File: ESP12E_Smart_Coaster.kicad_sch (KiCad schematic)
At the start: 33 parts, among them J1 SPI_Header, J2 MLX90614 Temp Sensor, J3 GPIO_Header, Q1 SI2302, SW1 SW_SPDT, SW2 SW_Push, U1 T6845C_Module, U2 ESP-12E, U3 AMS1117-3.3

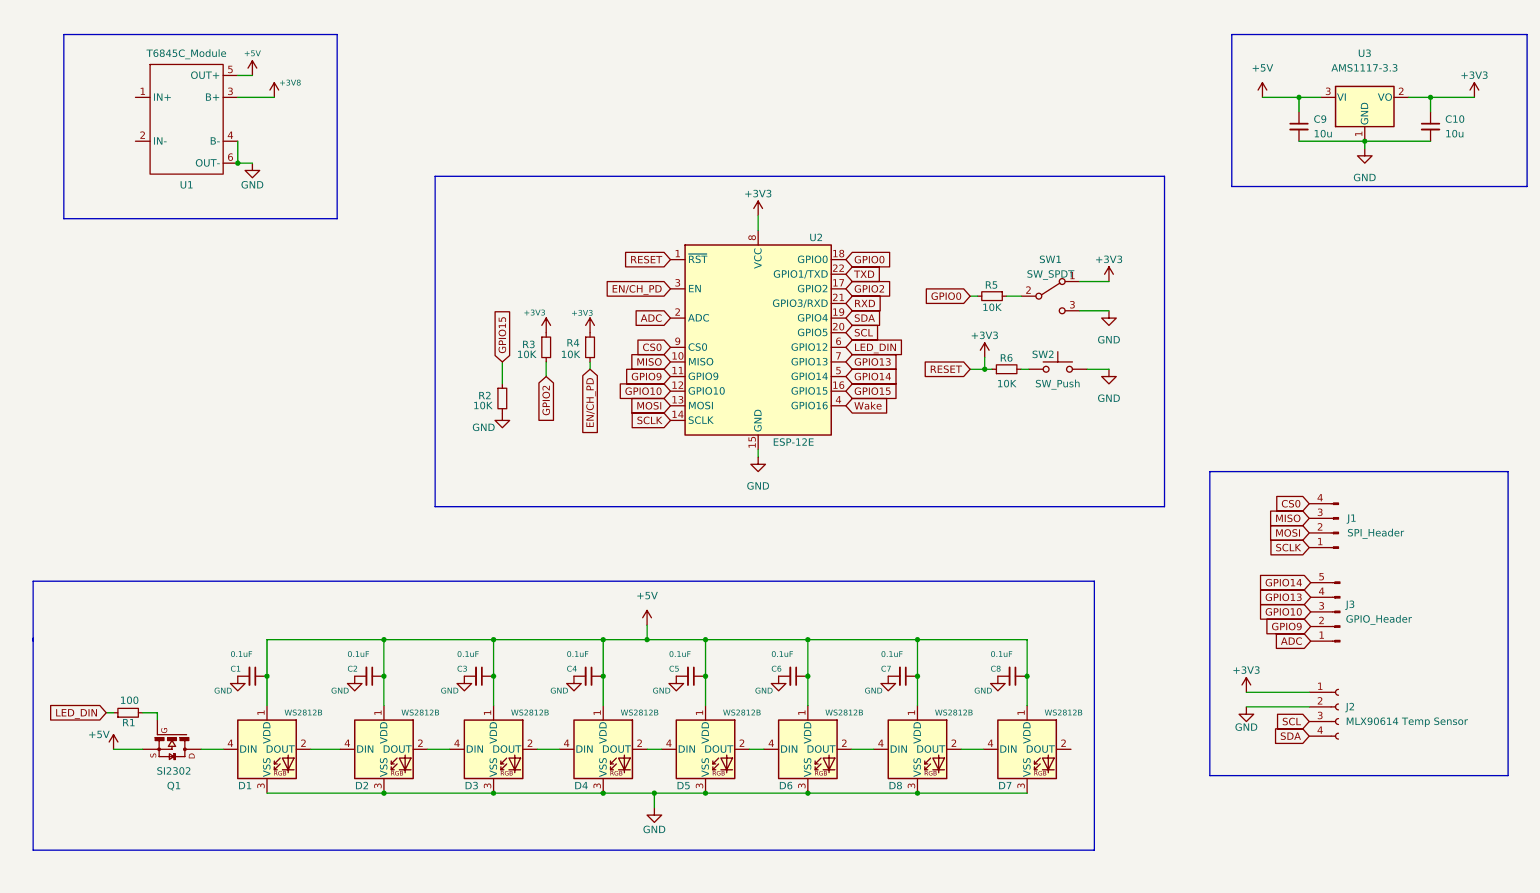
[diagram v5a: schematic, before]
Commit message: Started component placement
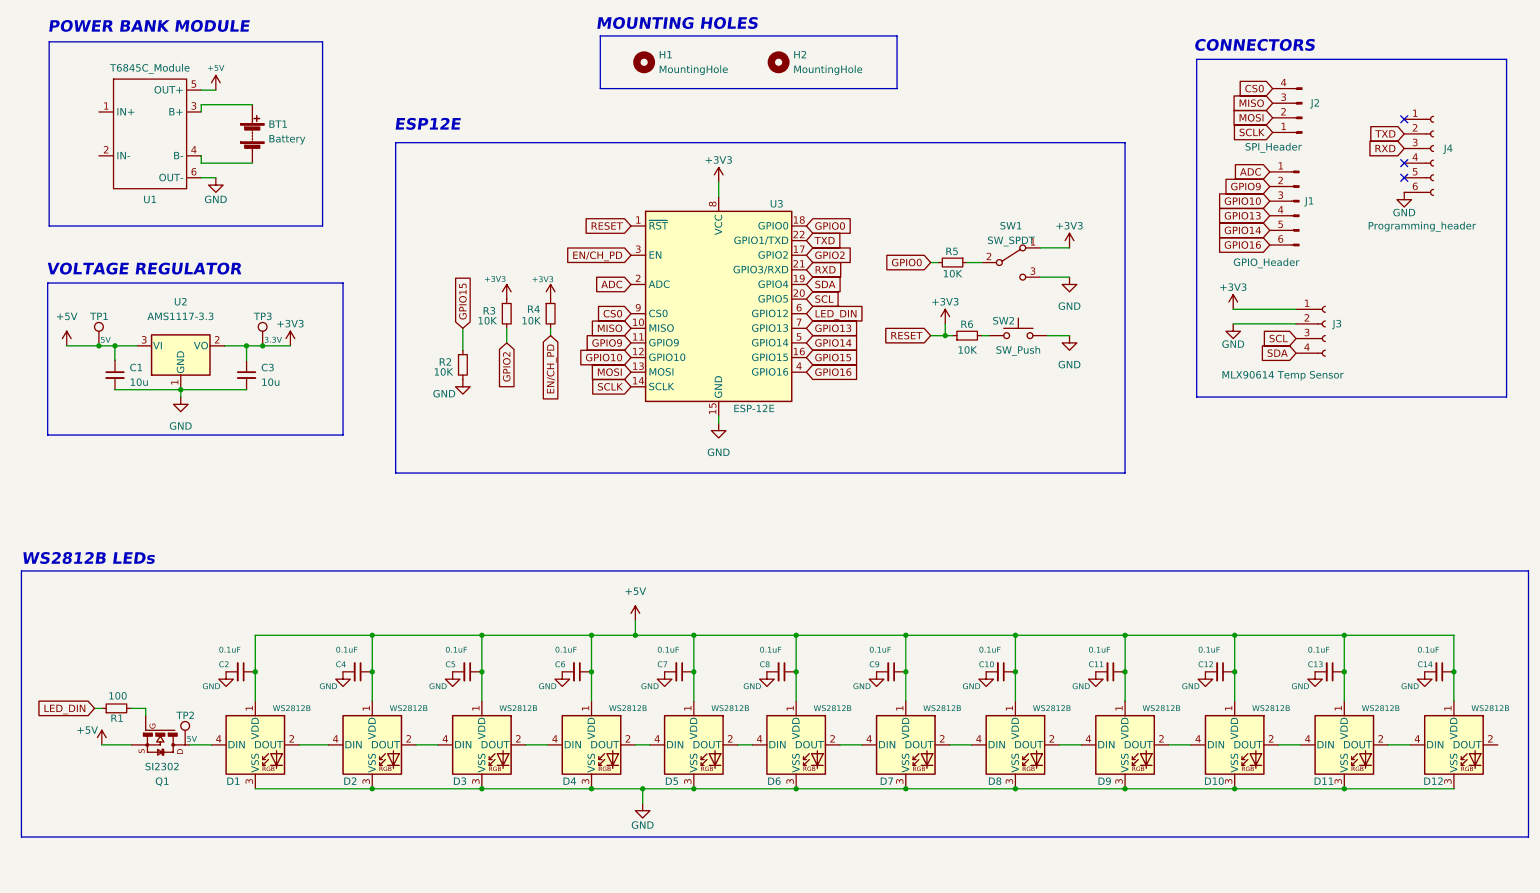
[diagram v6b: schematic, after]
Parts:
- removed J3: GPIO_Header, Connector_PinHeader_2.54mm:PinHeader_1x05_P2.54mm_Vertical, symbol Connector:Conn_01x05_Male
- added BT1: Battery, Battery:BatteryHolder_Keystone_1042_1x18650, symbol Device:Battery
- added C11, C12, C13, C14: 0.1uF, Capacitor_SMD:C_1206_3216Metric_Pad1.33x1.80mm_HandSolder, symbol Device:C_Small
- added D10, D11, D12, D9: WS2812B, LED_SMD:LED_WS2812B_PLCC4_5.0x5.0mm_P3.2mm, symbol LED:WS2812B
- added H1, H2: MountingHole, MountingHole:MountingHole_3.2mm_M3, symbol Mechanical:MountingHole
- added J1: GPIO_Header, Connector_PinHeader_2.54mm:PinHeader_1x06_P2.54mm_Vertical, symbol Connector:Conn_01x06_Male
- added J4: Programming_header, Connector_PinSocket_2.54mm:PinSocket_1x06_P2.54mm_Vertical, symbol Connector:Conn_01x06_Female
- added TP1, TP2: 5V, TestPoint:TestPoint_Loop_D2.54mm_Drill1.5mm_Beaded, symbol Connector:TestPoint
- added TP3: 3.3V, TestPoint:TestPoint_Loop_D2.54mm_Drill1.5mm_Beaded, symbol Connector:TestPoint
- J3: renamed from J2; footprint Connector_PinHeader_2.54mm:PinHeader_1x04_P2.54mm_Vertical -> Connector_JST:JST_XH_B4B-XH-A_1x04_P2.50mm_Vertical
- U1: footprint Button_Switch_SMD:SW_Push_SPST_NO_Alps_SKRK -> Power_Bank_Module:T6845C_Module
- renumbered C9 to C1, C8 to C10, C1 to C2, C10 to C3, C2 to C4, C3 to C5, C4 to C6, C5 to C7, C6 to C8, C7 to C9, J1 to J2, U3 to U2, U2 to U3
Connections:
- net +3V3: now also TP3.1
- net +5V: now also C11.1, C12.1, C13.1, C14.1, D10.1 (VDD), D11.1 (VDD), D12.1 (VDD), D9.1 (VDD), TP1.1
- net ADC: now also J1.1 (Pin_1)
- net GND: now also C11.2, C12.2, C13.2, C14.2, D10.3 (VSS), D11.3 (VSS), D12.3 (VSS), D9.3 (VSS), J4.6 (Pin_6); no longer U1.4 (B-)
- net GPIO10: now also J1.3 (Pin_3)
- net GPIO13: now also J1.4 (Pin_4)
- net GPIO14: now also J1.5 (Pin_5)
- net GPIO9: now also J1.2 (Pin_2)
- net RXD: now also J4.3 (Pin_3)
- net TXD: now also J4.2 (Pin_2)
- net at D8.2 (DOUT): now also D9.4 (DIN)
- net +3V8: no longer names the net of U1.3 (B+)
- net +3V8: now also BT1.1 (+)
- net Wake renamed GPIO16
- net GPIO16: now also J1.6 (Pin_6)
- new net: D11.2 (DOUT), D12.4 (DIN)
- new net: D10.2 (DOUT), D11.4 (DIN)
- new net: D10.4 (DIN), D9.2 (DOUT)
- new net: BT1.2 (-), U1.4 (B-)
- no-connect marks 0 -> 3
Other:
- note added: "CONNECTORS"
- note added: "ESP12E"
- note added: "MOUNTING HOLES"
- note added: "POWER BANK MODULE"
- note added: "VOLTAGE REGULATOR"
- note added: "WS2812B LEDs"
- moved on the sheet: C1, C10, C2, C3, C4, C5, C6, C7, C8, C9, D1, D2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

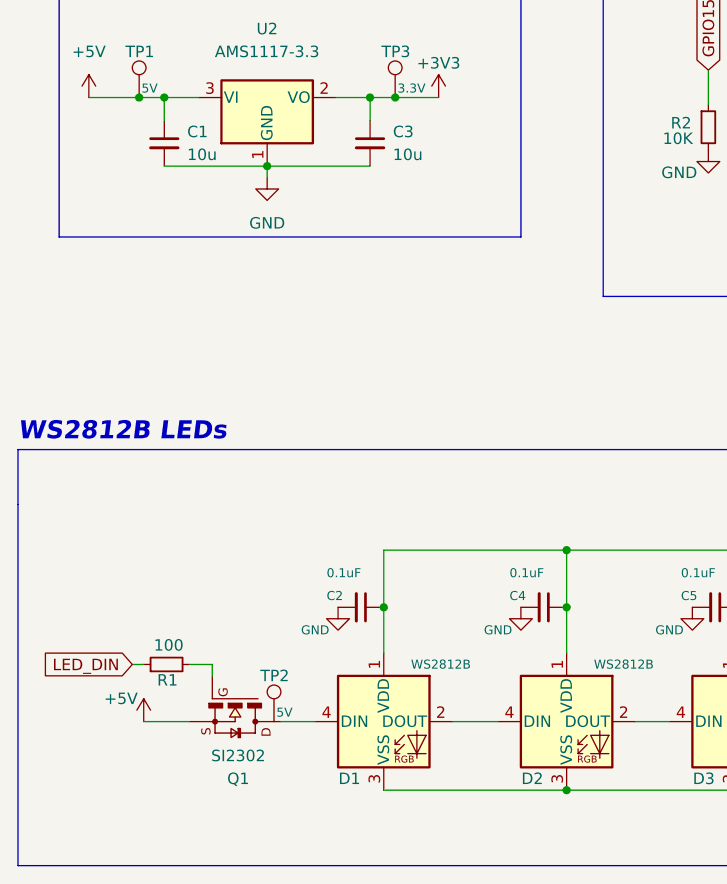
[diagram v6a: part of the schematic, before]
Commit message: Started PCB routing
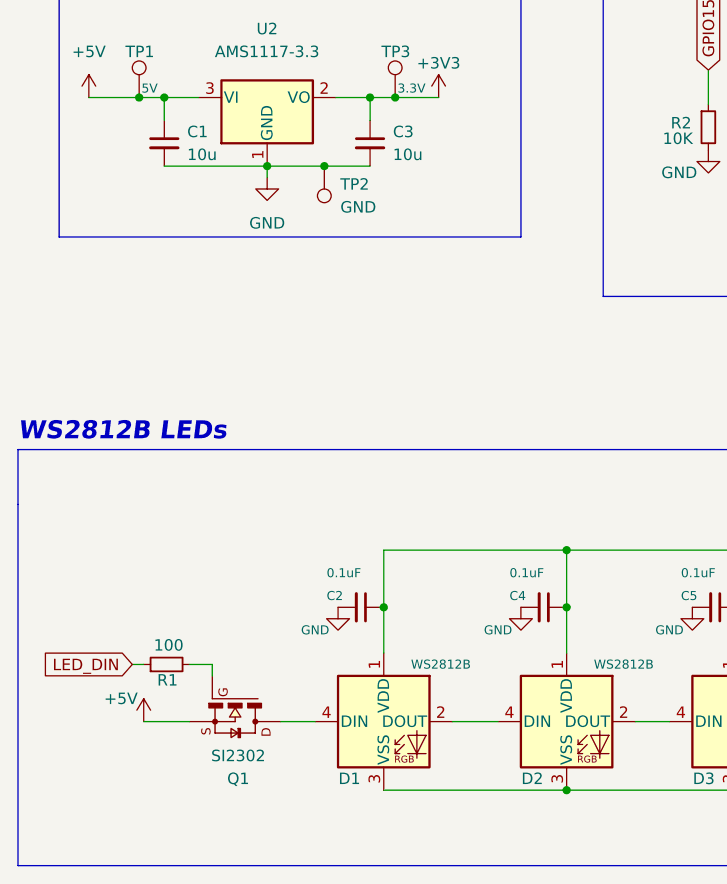
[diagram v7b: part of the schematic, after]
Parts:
- TP2: value 5V -> GND
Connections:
- net GND: now also TP2.1
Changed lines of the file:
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@@
   (junction (at 152.146 132.588) (diameter 0) (color 0 0 0 0)
+  )
+  (junction (at 51.562 83.566) (diameter 0) (color 0 0 0 0)
   )
   (junction (at 125.476 152.908) (diameter 0) (color 0 0 0 0)
@@
     (stroke (width 0) (type default) (color 0 0 0 0))
   )
+  (wire (pts (xy 51.562 83.566) (xy 56.642 83.566))
+    (stroke (width 0) (type default) (color 0 0 0 0))
+  )
   (polyline (pts (xy 73.406 91.44) (xy 73.406 65.024))
     (stroke (width 0) (type default) (color 0 0 0 0))
@@
     (stroke (width 0) (type default) (color 0 0 0 0))
   )
-  (wire (pts (xy 45.212 83.566) (xy 56.642 83.566))
+  (wire (pts (xy 45.212 83.566) (xy 51.562 83.566))
     (stroke (width 0) (type default) (color 0 0 0 0))
   )
@@
     (pin "2")
   )
+  (symbol (lib_id "Connector:TestPoint") (at 51.562 83.566 180) (unit 1)
+    (in_bom yes) (on_board yes) (fields_autoplaced)
+    (property "Reference" "TP2" (id 0) (at 53.34 85.5979 0)
+      (effects (font (size 1.27 1.27)) (justify right))
+    )
+    (property "Value" "GND" (id 1) (at 53.34 88.1379 0)
+      (effects (font (size 1.27 1.27)) (justify right))
+    )
+    (property "Footprint" "TestPoint:TestPoint_Loop_D2.54mm_Drill1.5mm_Beaded" (id 2) (at 46.482 83.566 0)
+      (effects (font (size 1.27 1.27)) hide)
+    )
+    (property "Datasheet" "~" (id 3) (at 46.482 83.566 0)
+      (effects (font (size 1.27 1.27)) hide)
+    )
+    (pin "1")
+  )
   (symbol (lib_id "LED:WS2812B") (at 58.166 145.288 0) (unit 1)
     (in_bom yes) (on_board yes)
@@
     )
     (property "Datasheet" "" (id 3) (at 199.644 58.928 0)
-      (effects (font (size 1.27 1.27)) hide)
-    )
-    (pin "1")
-  )
-  (symbol (lib_id "Connector:TestPoint") (at 45.974 145.288 0) (unit 1)
-    (in_bom yes) (on_board yes)
-    (property "Reference" "TP2" (id 0) (at 44.45 140.208 0)
-      (effects (font (size 1.27 1.27)) (justify left))
-    )
-    (property "Value" "5V" (id 1) (at 46.228 144.272 0)
-      (effects (font (size 1 1)) (justify left))
-    )
-    (property "Footprint" "TestPoint:TestPoint_Loop_D2.54mm_Drill1.5mm_Beaded" (id 2) (at 51.054 145.288 0)
-      (effects (font (size 1.27 1.27)) hide)
-    )
-    (property "Datasheet" "~" (id 3) (at 51.054 145.288 0)
       (effects (font (size 1.27 1.27)) hide)
     )
@@
       (reference "TP1") (unit 1) (value "5V") (footprint "TestPoint:TestPoint_Loop_D2.54mm_Drill1.5mm_Beaded")
     )
-    (path "/4ab6093e-85ca-41d6-ae5c-2fec8c9b2ffd"
-      (reference "TP2") (unit 1) (value "5V") (footprint "TestPoint:TestPoint_Loop_D2.54mm_Drill1.5mm_Beaded")
+    (path "/3c64e79d-7cd7-4467-a8ee-31a3955953f4"
+      (reference "TP2") (unit 1) (value "GND") (footprint "TestPoint:TestPoint_Loop_D2.54mm_Drill1.5mm_Beaded")
     )
     (path "/64b64b1b-b0d3-4ebe-aca8-3b831d2199db"

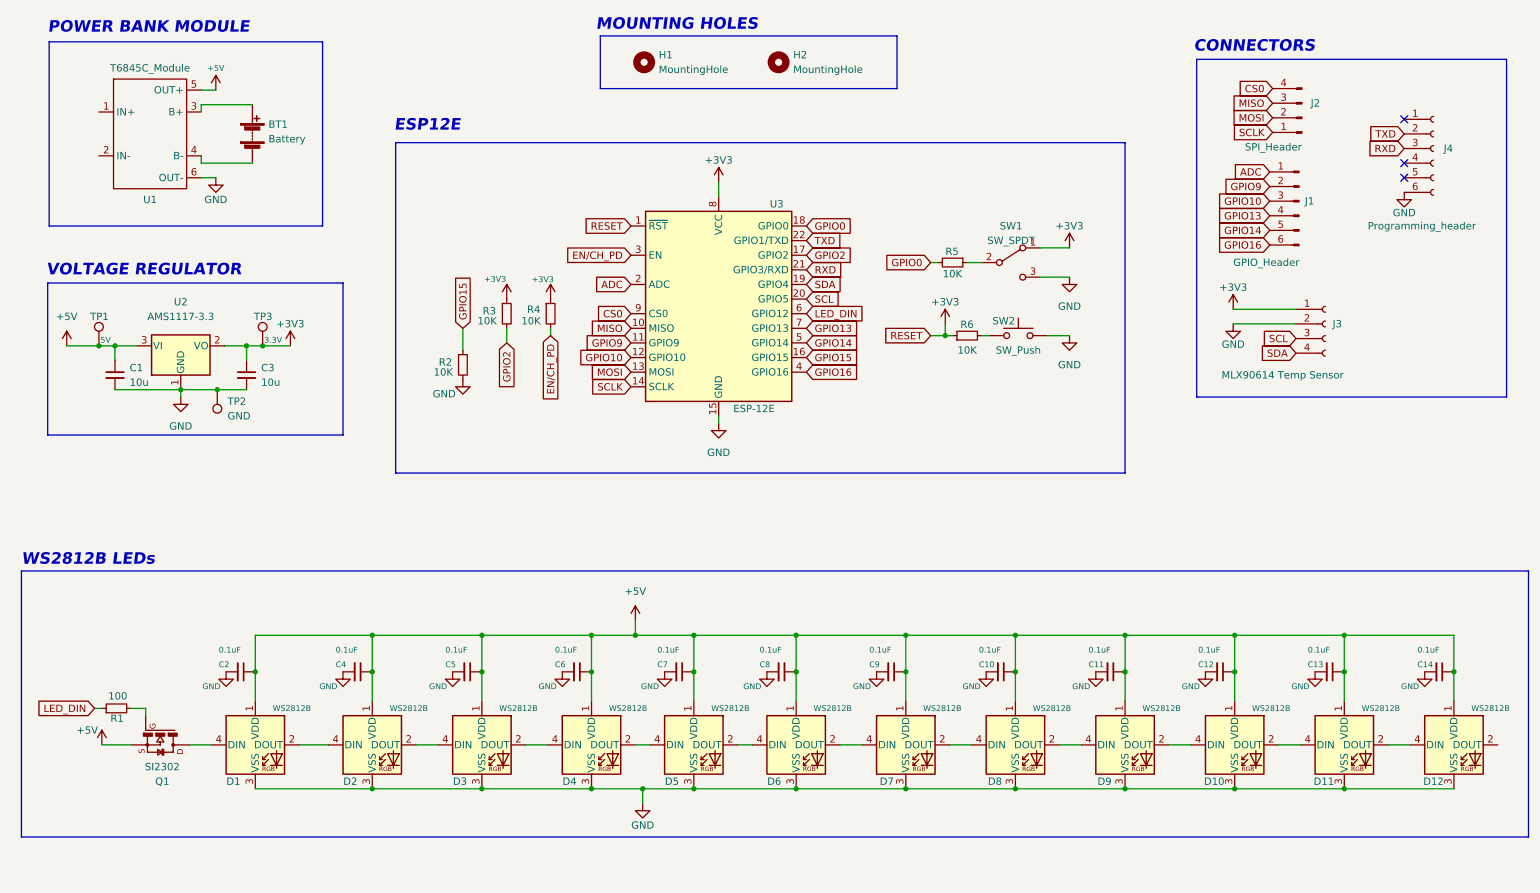
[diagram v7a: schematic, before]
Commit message: Added power connector and wake jumper
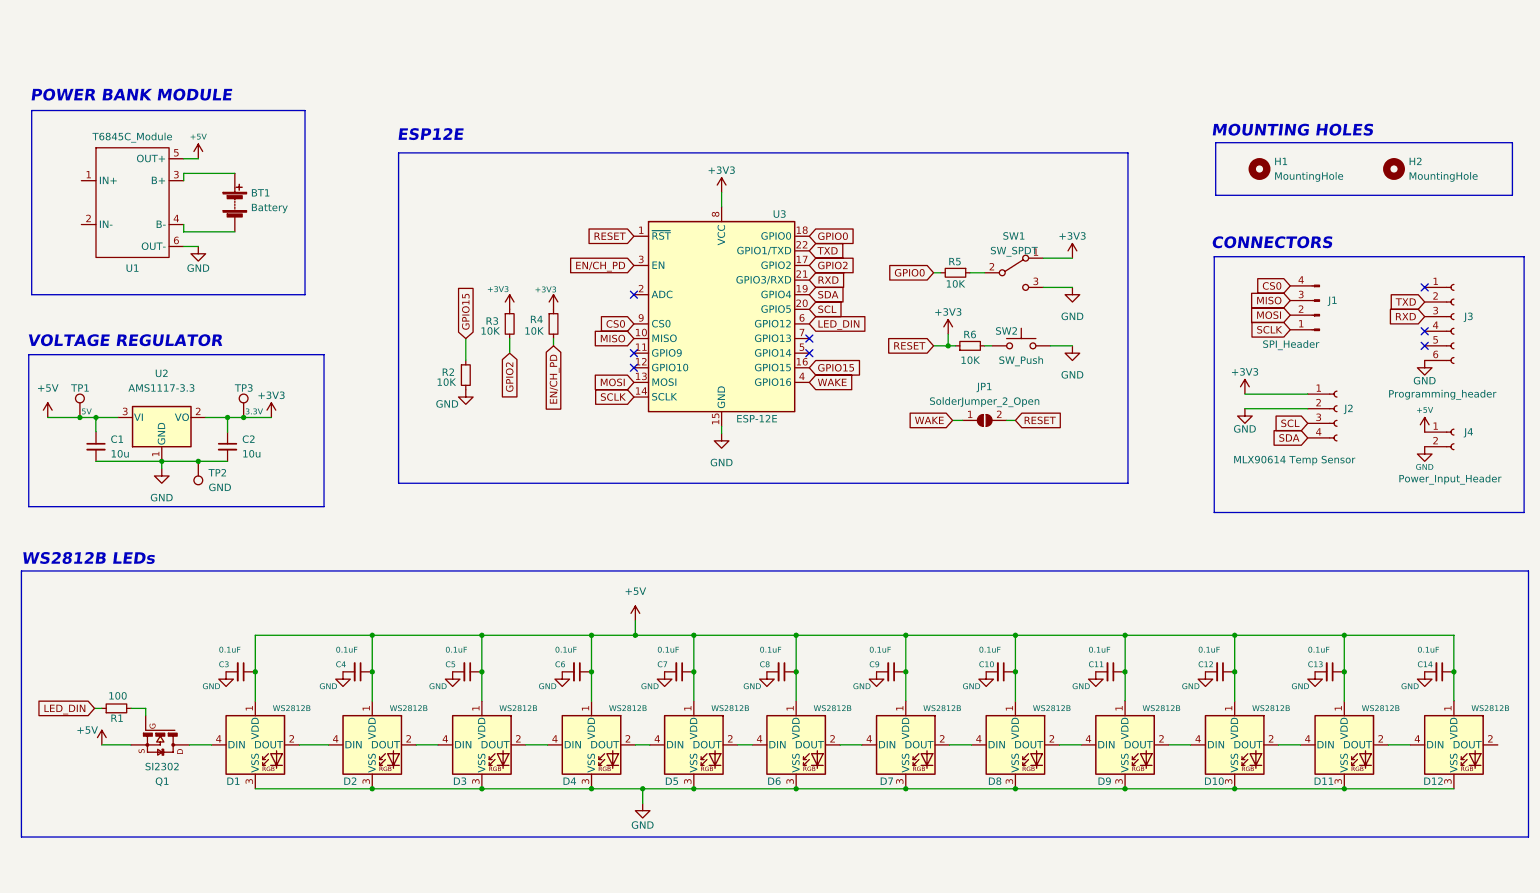
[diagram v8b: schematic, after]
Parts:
- removed J1: GPIO_Header, Connector_PinHeader_2.54mm:PinHeader_1x06_P2.54mm_Vertical, symbol Connector:Conn_01x06_Male
- added J4: Power_Input_Header, Connector_JST:JST_XH_B2B-XH-A_1x02_P2.50mm_Vertical, symbol Connector:Conn_01x02_Female
- added JP1: SolderJumper_2_Open, Connector_PinHeader_2.54mm:PinHeader_1x02_P2.54mm_Vertical, symbol Jumper:SolderJumper_2_Open
- renumbered C3 to C2, C2 to C3, J2 to J1, J3 to J2, J4 to J3
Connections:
- net +3V3: now also JP1.2 (B)
- net +5V: now also J4.1 (Pin_1)
- net GND: now also J4.2 (Pin_2)
- net ADC: no longer names the net of U3.2 (ADC)
- net GPIO10: no longer names the net of U3.12 (GPIO10)
- net GPIO13: no longer names the net of U3.7 (GPIO13)
- net GPIO14: no longer names the net of U3.5 (GPIO14)
- net GPIO16 renamed WAKE
- net WAKE: now also JP1.1 (A)
- net GPIO9: no longer names the net of U3.11 (GPIO9)
- no-connect marks 3 -> 8
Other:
- moved on the sheet: BT1, C1, C2, H1, H2, J1, J2, J3, R2, R3, R4, R5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
